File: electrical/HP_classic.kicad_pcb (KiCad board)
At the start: 2 copper layers, 56 x 40 mm, 15 parts, among them J1 USB_B_Micro, J2 JST PH 2mm, J3 2.54mm R/A, U1 MCP73831-2-OT

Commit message: Version 1 Checkin
Schematic updated with component details
PCB udpated for plot formatting
Check plots generated
Interactive BOM generated
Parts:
- R2: value 470 -> 820

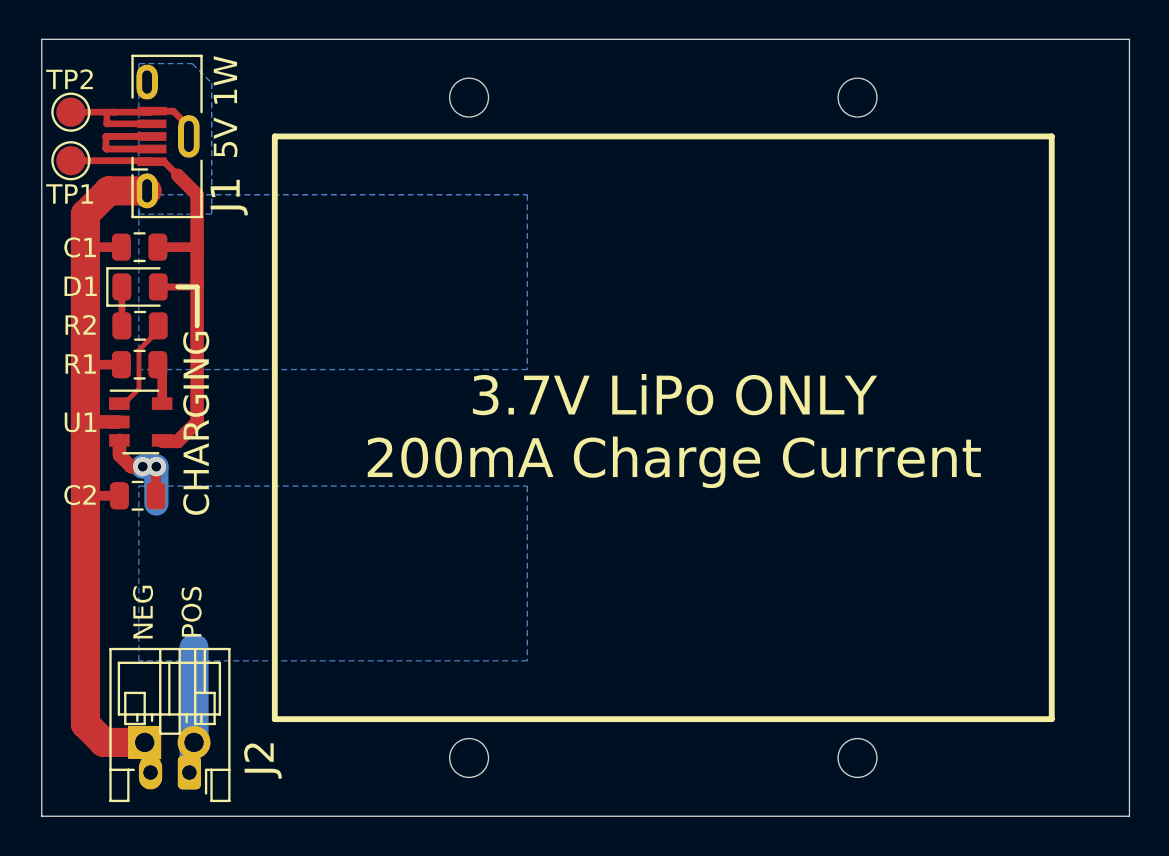
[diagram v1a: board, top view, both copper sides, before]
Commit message: upload version 2 ecad and updates
Upload of v2 KiCad schematic, PCB, and BOM information. V2 includes protection circuitry to prevent damage if an HP charger is attached while this pack is installed in the calculator.
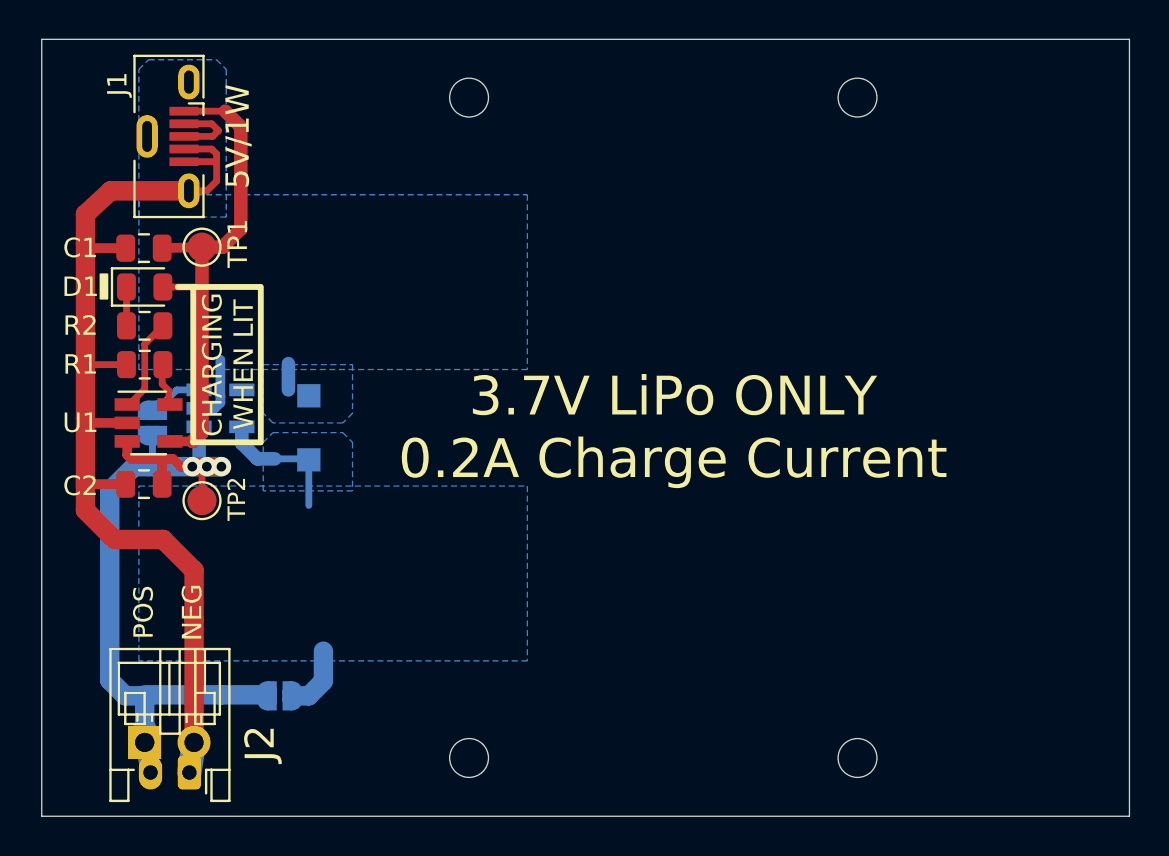
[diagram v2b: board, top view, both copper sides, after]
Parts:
- added JP1: BYPASS, Jumper:SolderJumper-2_P1.3mm_Open_RoundedPad1.0x1.5mm, B.Cu at (159.2, 138.8)
- added JP2: ENABLE, Jumper:SolderJumper-2_P1.3mm_Open_RoundedPad1.0x1.5mm, B.Cu at (152.7, 124.8)
- added U2: MAX40203AUK, Package_TO_SOT_SMD:SOT-23-5, B.Cu at (156.2, 124.0)
- added Z1: MMBZ5231, Diode_SMD:D_SOD-123, B.Cu at (160.8, 125.0)
- R1: value 5.1K -> 4.7K
- R2: value 820 -> 470
- TP2: value GND -> VBAT
- moved TP2 21.1 mm to (155.2, 128.8)
- moved TP1 8.08 mm to (155.2, 115.7)
- moved C2 0.68 mm to (152.3, 127.9)
- moved U1 0.40 mm to (152.5, 124.8)
- moved R1 0.26 mm to (152.3, 121.8)
- moved D1 0.24 mm to (152.3, 117.8)
- moved R2 0.24 mm to (152.3, 119.8)
- moved C1 0.23 mm to (152.3, 115.8)
- turned J1 to 270 degrees
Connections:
- J2 pad 1: /VBAT -> GND
- J2 pad 2: GND -> /VBAT
- J3 pad 1: GND -> /VBAT
- J3 pad 2: /VBAT -> GND
- TP2 pad 1: GND -> /VBAT
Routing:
- net /VBAT: track 13.5 -> 42.8 mm, vias 2 -> 3
- net /POS: track 0.00 -> 10.3 mm
- net GND: track 52.6 -> 59.4 mm
- net Net-(JP2-Pad2): track 0.00 -> 2.90 mm
- net Net-(J1-Pad2): track 5.37 -> 3.82 mm
- net /VUSB: track 25.2 -> 26.6 mm
- added copper zone on B.Cu, net /POS
- removed copper zone on B.Cu, net /VBAT
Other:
- board text added: "3.7V LiPo ONLY 0.2A Charge Current"
- board text added: "5V/1W"
- board text added: "CHARGING WHEN LIT"
- board text added: "HP CLASSIC CALCULATOR LiPo BATTERY SUPPLY"
- board text added: "V2 12/2020"
- board text added: "https://hackaday.io/project/175815 tomcircuit@gmail.com"
- board text removed: "3.7V LiPo ONLY 200mA Charge Current"
- board text removed: "5V 1W"
- board text removed: "CHARGING"
- board text removed: "CLASSIC HP CALCULATOR LiPo BATTERY SUPPLY"
- board text removed: "V1 11/2020 https://hackaday.io/project/175815 tomcircuit@gmail.com"
